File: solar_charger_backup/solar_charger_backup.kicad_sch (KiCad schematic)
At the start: 16 parts, among them U1 LT3652HVIMSE#PBF, U2 LM234Z-3

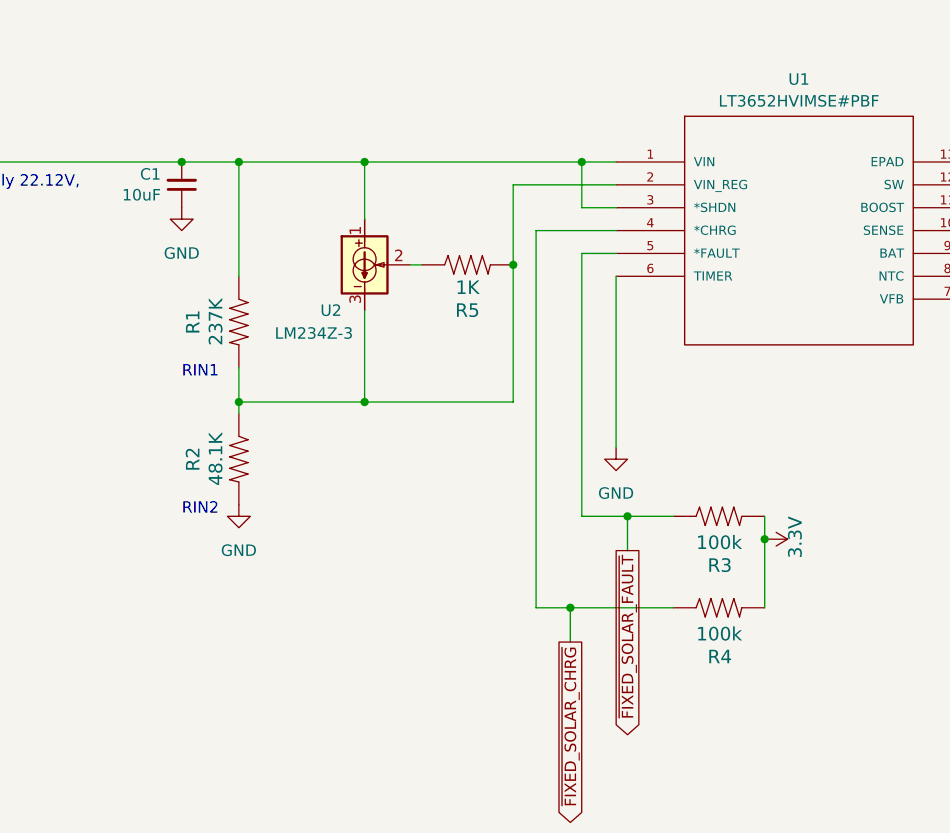
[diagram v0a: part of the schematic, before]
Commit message: updated with durand-groundstation components, cleaned up libraries
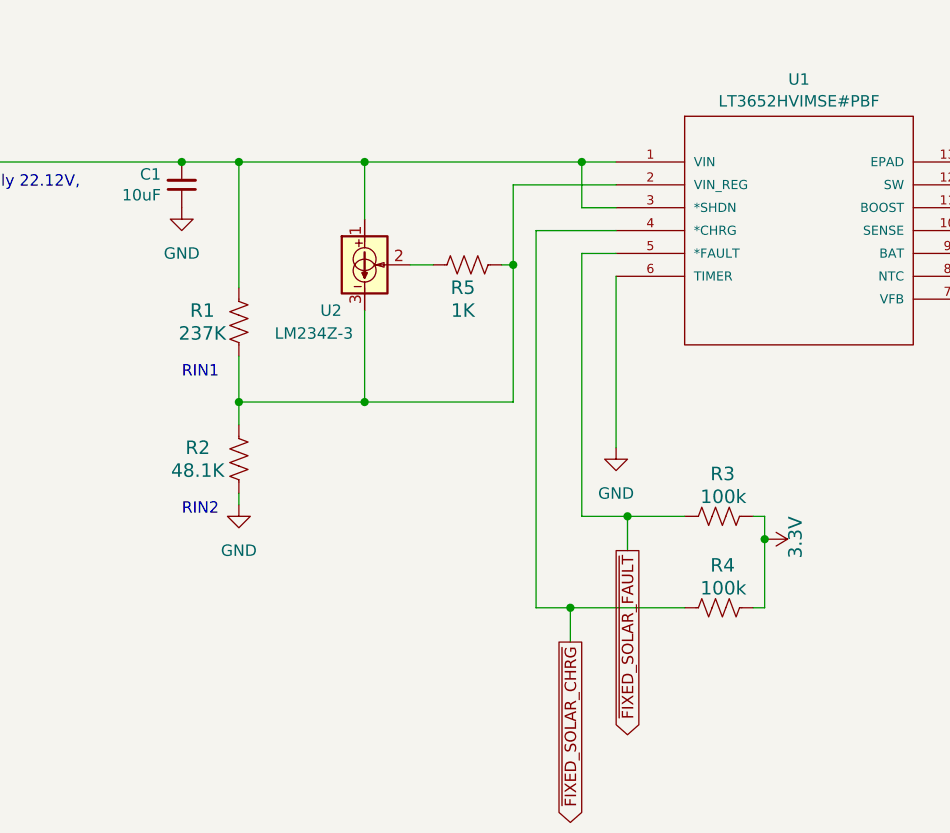
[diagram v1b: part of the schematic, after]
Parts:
- R1, R2, R3, R4, R5: symbol mainboard:R-US_R0603 -> Device:R_US
